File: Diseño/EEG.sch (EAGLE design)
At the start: 32 parts, among them IC1 REF2033AIDDCT, IC2 MCP73831T-2ACI_OT, IC3 LP38692MP-3.3_NOPB, X1 MINI-USB_4P-85-32004-40X

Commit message: correcciones
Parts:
- removed X1: MINI-USB_4P-85-32004-40X, con-cypressindustries:MINI-USB_4P-85-32004-40X
- added J1: USB3500-30-A-KIT, USB3500-30-A-KIT:USB3500-30-A-KIT
- added J2: SJ3-35083A-TR, SJ3-35083A-TR:SJ3-35083A-TR
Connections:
- new net CS1: INA_1.-IN, J2.TIP
- new net CS2: INA_1.+IN, J2.RING
- net +BATT: no longer X1.1
- net GND: now also J1.MH1, J1.MH2, J1.MH3, J1.MH4, J2.SLEEVE; no longer X1.4
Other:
- moved on the sheet: C1, C3, IC2, LED1, R1, R2

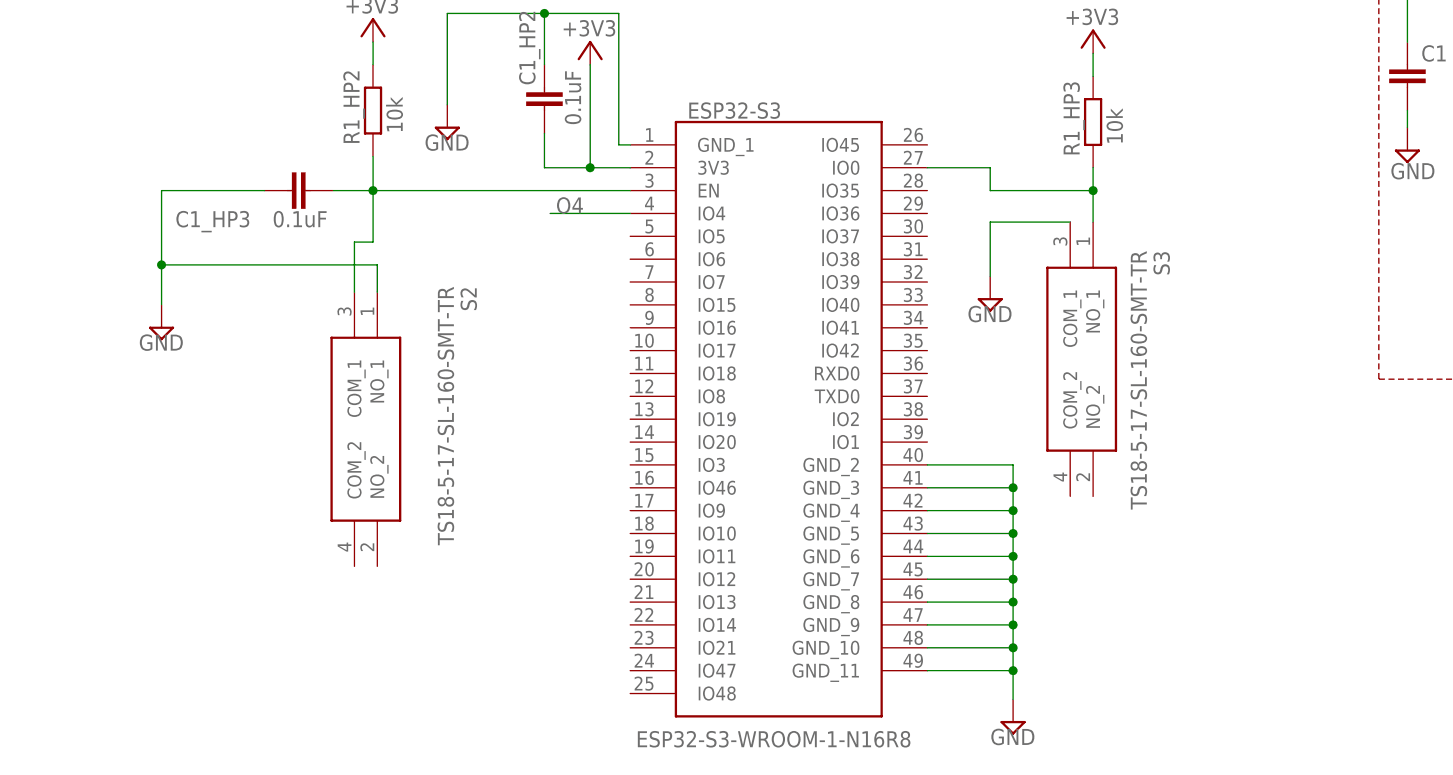
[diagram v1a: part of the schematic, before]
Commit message: Se actualizo el diagrama de la ESP 32-S3
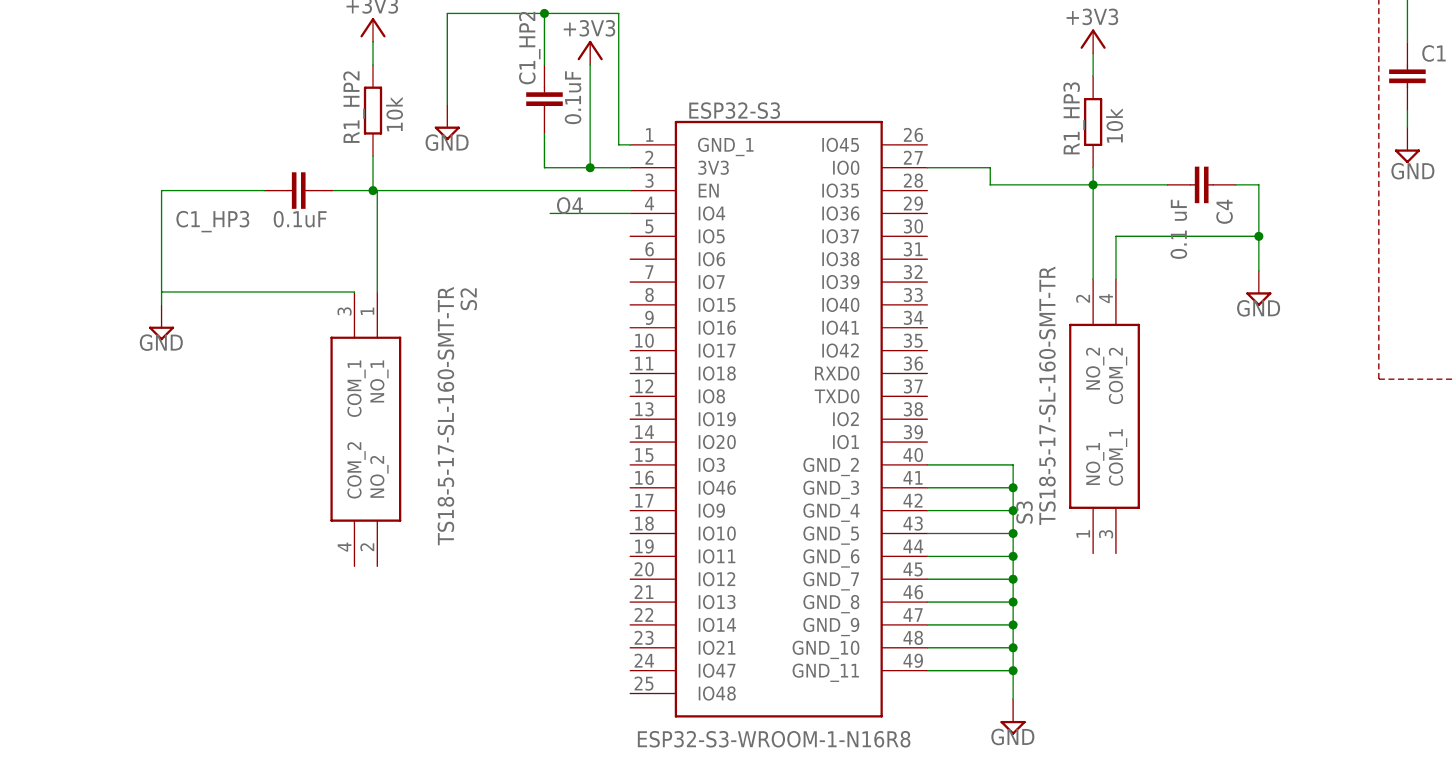
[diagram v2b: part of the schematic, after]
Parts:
- added C4: 0.1 uF, rcl:C-EUC0805
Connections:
- net GND: now also C4.1, S2.COM_1, S3.COM_2; no longer S2.NO_1, S3.COM_1
- net N$13: now also C4.2, S3.NO_2; no longer S3.NO_1
- net N$15: now also S2.NO_1; no longer S2.COM_1
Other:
- moved on the sheet: S3
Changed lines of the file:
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@@
 <part name="SUPPLY15" library="supply2" library_urn="urn:adsk.eagle:library:372" deviceset="GND" device=""/>
 <part name="GND6" library="supply2" library_urn="urn:adsk.eagle:library:372" deviceset="GND" device=""/>
+<part name="C4" library="rcl" library_urn="urn:adsk.eagle:library:334" deviceset="C-EU" device="C0805" package3d_urn="urn:adsk.eagle:package:23617/2" value="0.1 uF"/>
 </parts>
 <sheets>
@@
 <attribute name="VALUE" x="48.73625" y="61.11875" size="1.778" layer="96" rot="R270" align="center-left"/>
 </instance>
-<instance part="S3" gate="G$1" x="120.65" y="68.2625" smashed="yes" rot="R270">
-<attribute name="NAME" x="128.27" y="65.0875" size="1.778" layer="95" rot="R270" align="center-left"/>
-<attribute name="VALUE" x="125.73" y="65.0875" size="1.778" layer="96" rot="R270" align="center-left"/>
+<instance part="S3" gate="G$1" x="120.65" y="31.4325" smashed="yes" rot="R90">
+<attribute name="NAME" x="113.03" y="34.6075" size="1.778" layer="95" rot="R90" align="center-left"/>
+<attribute name="VALUE" x="115.57" y="34.6075" size="1.778" layer="96" rot="R90" align="center-left"/>
 </instance>
 <instance part="R1_HP2" gate="G$1" x="40.64" y="80.645" smashed="yes" rot="R90">
@@
 <attribute name="VALUE" x="117.475" y="90.17" size="1.778" layer="96"/>
 </instance>
-<instance part="GND4" gate="GND" x="109.22" y="59.69" smashed="yes">
-<attribute name="VALUE" x="106.68" y="57.15" size="1.778" layer="96"/>
+<instance part="GND4" gate="GND" x="139.065" y="60.325" smashed="yes">
+<attribute name="VALUE" x="136.525" y="57.785" size="1.778" layer="96"/>
 </instance>
 <instance part="GND5" gate="GND" x="111.76" y="12.7" smashed="yes">
@@
 <instance part="GND6" gate="GND" x="8.89" y="137.795" smashed="yes">
 <attribute name="VALUE" x="6.35" y="135.255" size="1.778" layer="96"/>
+</instance>
+<instance part="C4" gate="G$1" x="133.985" y="72.39" smashed="yes" rot="R270">
+<attribute name="NAME" x="134.366" y="70.866" size="1.778" layer="95" rot="R270"/>
+<attribute name="VALUE" x="129.286" y="70.866" size="1.778" layer="96" rot="R270"/>
 </instance>
 </instances>
@@
 <pinref part="GND3" gate="GND" pin="GND"/>
 <wire x1="28.575" y1="71.755" x2="17.145" y2="71.755" width="0.1524" layer="91"/>
-<wire x1="17.145" y1="71.755" x2="17.145" y2="63.5" width="0.1524" layer="91"/>
-<pinref part="S2" gate="G$1" pin="NO_1"/>
-<wire x1="17.145" y1="63.5" x2="17.145" y2="59.055" width="0.1524" layer="91"/>
-<wire x1="41.11625" y1="60.48375" x2="41.11625" y2="63.5" width="0.1524" layer="91"/>
-<wire x1="41.11625" y1="63.5" x2="17.145" y2="63.5" width="0.1524" layer="91"/>
-<junction x="17.145" y="63.5"/>
-</segment>
-<segment>
-<pinref part="S3" gate="G$1" pin="COM_1"/>
-<wire x1="118.11" y1="68.2625" x2="109.22" y2="68.2625" width="0.1524" layer="91"/>
-<pinref part="GND4" gate="GND" pin="GND"/>
-<wire x1="109.22" y1="68.2625" x2="109.22" y2="62.23" width="0.1524" layer="91"/>
+<wire x1="17.145" y1="71.755" x2="17.145" y2="60.48375" width="0.1524" layer="91"/>
+<pinref part="S2" gate="G$1" pin="COM_1"/>
+<wire x1="17.145" y1="60.325" x2="17.145" y2="59.055" width="0.1524" layer="91"/>
+<wire x1="38.57625" y1="60.48375" x2="17.145" y2="60.48375" width="0.1524" layer="91"/>
+<wire x1="17.145" y1="60.48375" x2="17.145" y2="60.325" width="0.1524" layer="91"/>
 </segment>
 <segment>
@@
 <wire x1="18.415" y1="141.605" x2="8.89" y2="141.605" width="0.1524" layer="91"/>
 </segment>
+<segment>
+<pinref part="GND4" gate="GND" pin="GND"/>
+<pinref part="C4" gate="G$1" pin="1"/>
+<wire x1="139.065" y1="62.865" x2="139.065" y2="66.675" width="0.1524" layer="91"/>
+<wire x1="139.065" y1="66.675" x2="139.065" y2="72.39" width="0.1524" layer="91"/>
+<wire x1="139.065" y1="72.39" x2="136.525" y2="72.39" width="0.1524" layer="91"/>
+<pinref part="S3" gate="G$1" pin="COM_2"/>
+<wire x1="123.19" y1="61.9125" x2="123.19" y2="66.675" width="0.1524" layer="91"/>
+<wire x1="123.19" y1="66.675" x2="139.065" y2="66.675" width="0.1524" layer="91"/>
+<junction x="139.065" y="66.675"/>
+</segment>
 </net>
 <net name="N$1" class="0">
@@
 <pinref part="R1_HP2" gate="G$1" pin="1"/>
 <wire x1="40.64" y1="71.755" x2="40.64" y2="75.565" width="0.1524" layer="91"/>
-<pinref part="S2" gate="G$1" pin="COM_1"/>
-<wire x1="38.57625" y1="60.48375" x2="38.57625" y2="66.04" width="0.1524" layer="91"/>
-<wire x1="38.57625" y1="66.04" x2="40.64" y2="66.04" width="0.1524" layer="91"/>
-<wire x1="40.64" y1="66.04" x2="40.64" y2="71.755" width="0.1524" layer="91"/>
-</segment>
-</net>
-<net name="N$13" class="0">
-<segment>
-<pinref part="S3" gate="G$1" pin="NO_1"/>
-<pinref part="R1_HP3" gate="G$1" pin="1"/>
-<wire x1="120.65" y1="68.2625" x2="120.65" y2="71.755" width="0.1524" layer="91"/>
-<pinref part="ESP32-S3" gate="G$1" pin="IO0"/>
-<wire x1="120.65" y1="71.755" x2="120.65" y2="74.295" width="0.1524" layer="91"/>
-<wire x1="102.235" y1="74.295" x2="109.22" y2="74.295" width="0.1524" layer="91"/>
-<wire x1="109.22" y1="74.295" x2="109.22" y2="71.755" width="0.1524" layer="91"/>
-<wire x1="109.22" y1="71.755" x2="120.65" y2="71.755" width="0.1524" layer="91"/>
-<junction x="120.65" y="71.755"/>
+<pinref part="S2" gate="G$1" pin="NO_1"/>
+<wire x1="41.11625" y1="60.48375" x2="41.11625" y2="71.755" width="0.1524" layer="91"/>
+<wire x1="41.11625" y1="71.755" x2="40.64" y2="71.755" width="0.1524" layer="91"/>
 </segment>
 </net>
@@
 </segment>
 </net>
+<net name="N$13" class="0">
+<segment>
+<pinref part="ESP32-S3" gate="G$1" pin="IO0"/>
+<wire x1="102.235" y1="74.295" x2="109.22" y2="74.295" width="0.1524" layer="91"/>
+<wire x1="109.22" y1="74.295" x2="109.22" y2="72.39" width="0.1524" layer="91"/>
+<pinref part="C4" gate="G$1" pin="2"/>
+<wire x1="109.22" y1="72.39" x2="120.65" y2="72.39" width="0.1524" layer="91"/>
+<wire x1="120.65" y1="72.39" x2="128.905" y2="72.39" width="0.1524" layer="91"/>
+<junction x="120.65" y="72.39"/>
+<pinref part="R1_HP3" gate="G$1" pin="1"/>
+<wire x1="120.65" y1="74.295" x2="120.65" y2="72.39" width="0.1524" layer="91"/>
+<pinref part="S3" gate="G$1" pin="NO_2"/>
+<wire x1="120.65" y1="61.9125" x2="120.65" y2="72.39" width="0.1524" layer="91"/>
+</segment>
+</net>

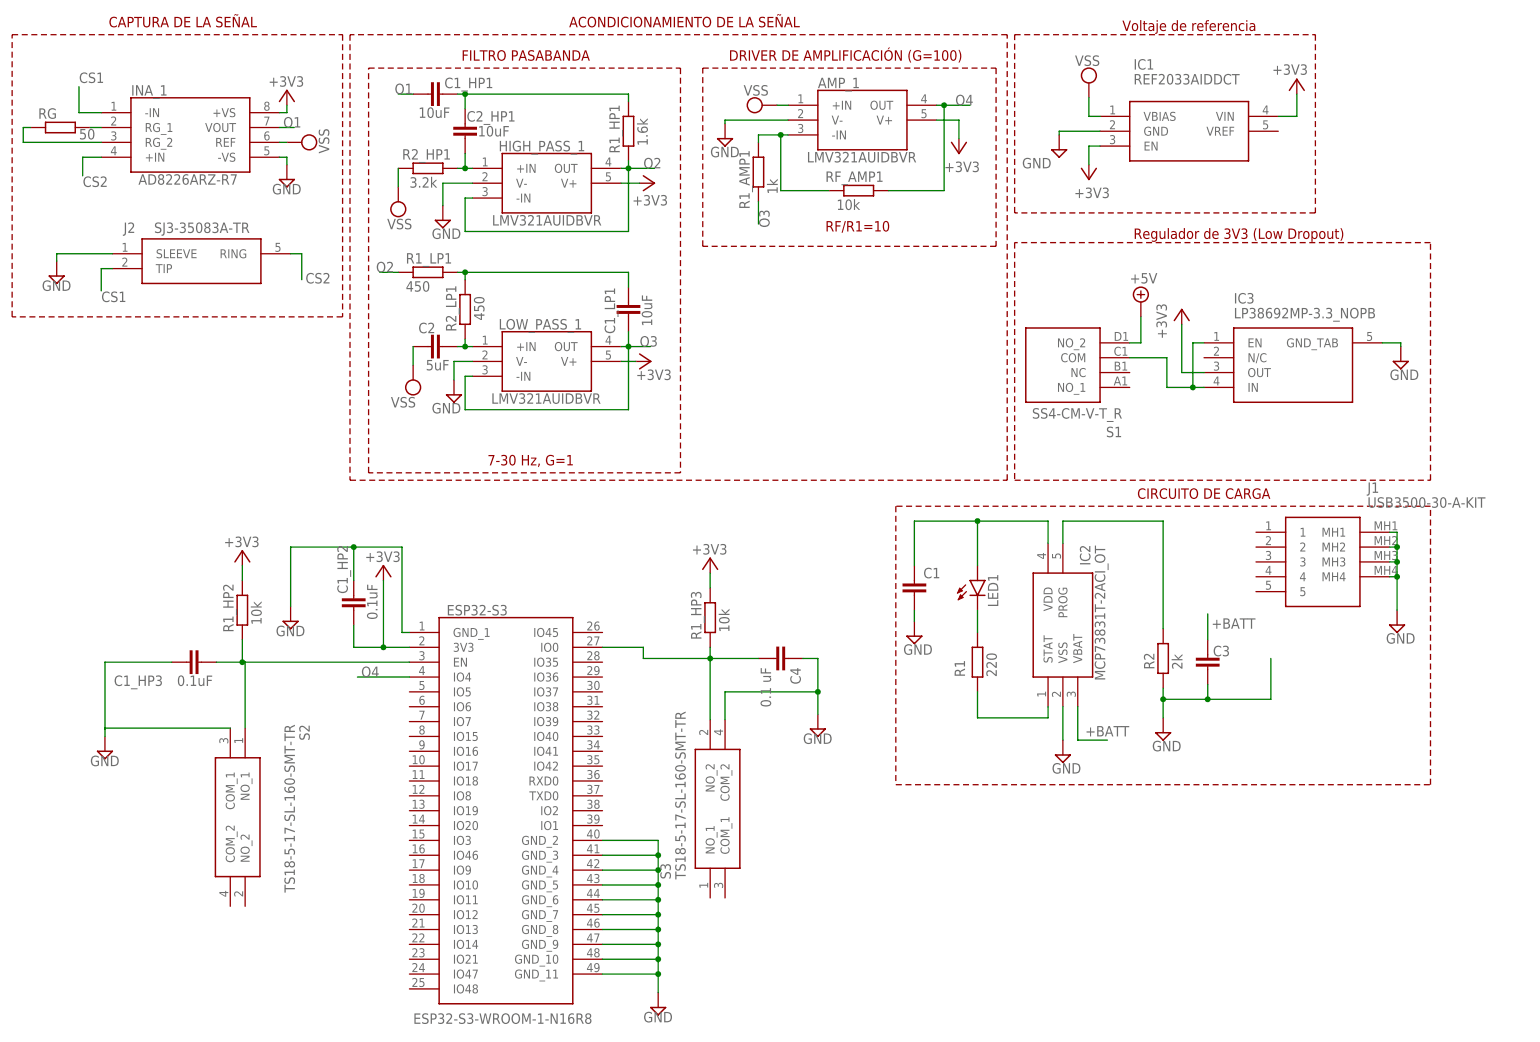
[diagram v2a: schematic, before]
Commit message: mod circuito de carga, amplificadores y filtros
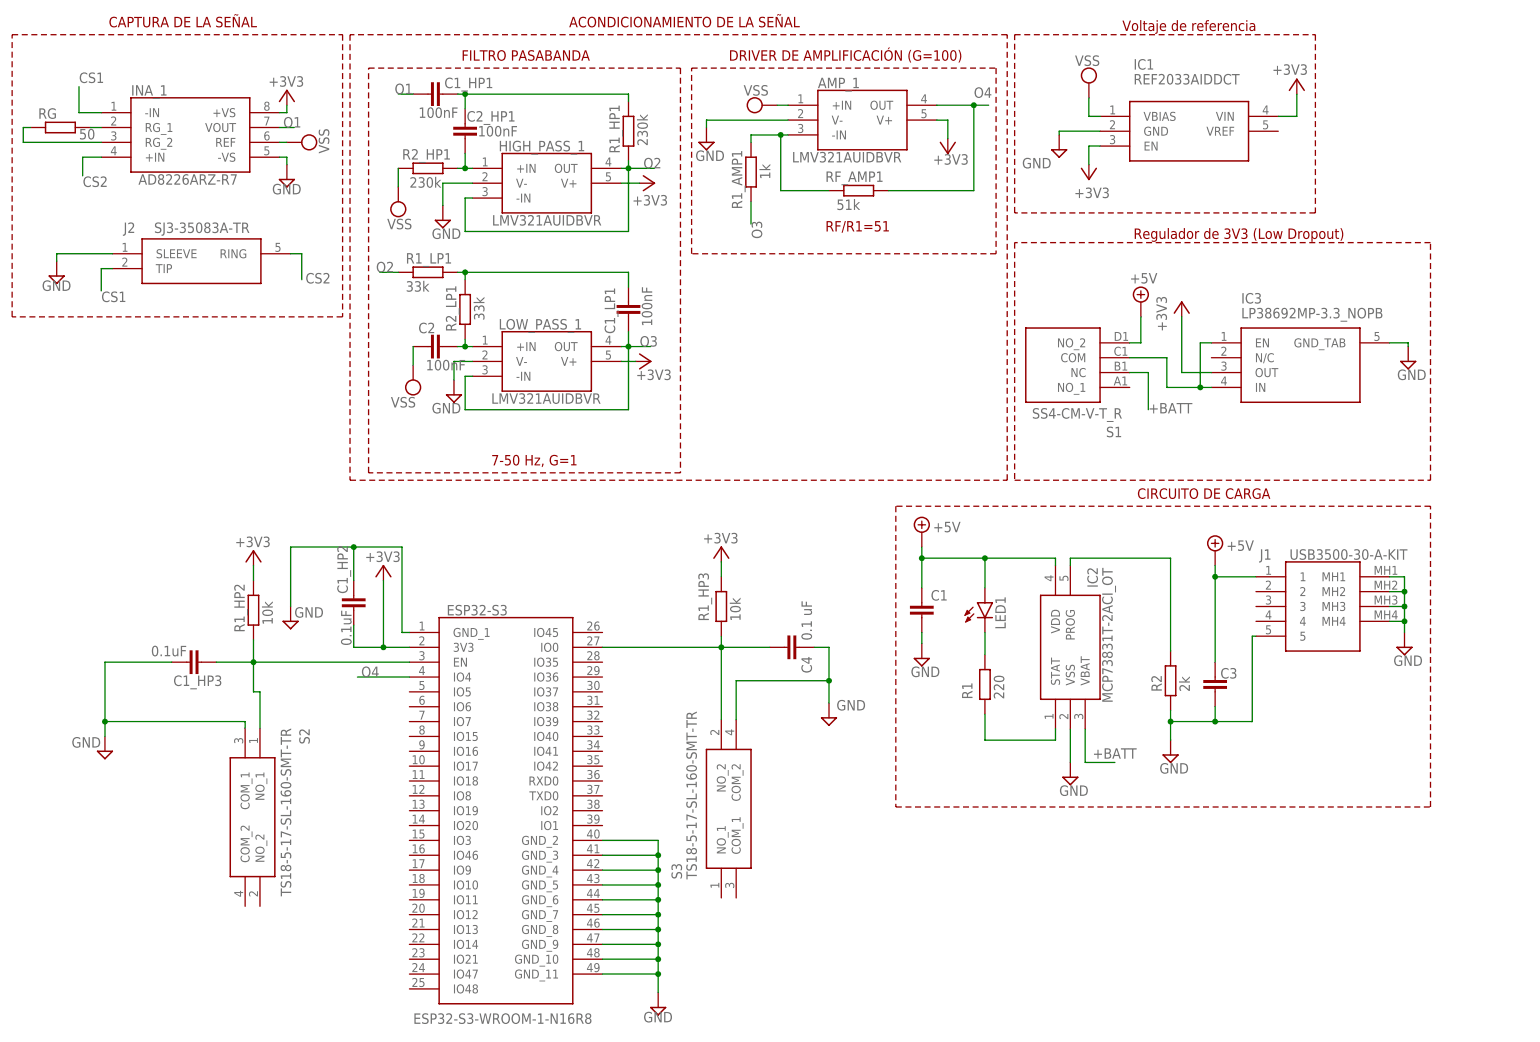
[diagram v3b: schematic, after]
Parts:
- C1_HP1, C1_LP1, C2_HP1: value 10uF -> 100nF
- C2: value 5uF -> 100nF
- R1_HP1: value 1.6k -> 230k
- R1_LP1, R2_LP1: value 450 -> 33k
- R2_HP1: value 3.2k -> 230k
- RF_AMP1: value 10k -> 51k
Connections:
- removed net N$1: C1.1, IC2.VDD, LED1.A
- net +5V: now also C1.1, C3.1, IC2.VDD, J1.1, LED1.A
- net +BATT: now also S1.NC; no longer C3.1
- net GND: now also J1.5
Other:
- note added: "7-50 Hz, G=1"
- note added: "RF/R1=51"
- note removed: "7-30 Hz, G=1"
- note removed: "RF/R1=10"
- moved on the sheet: C1, C3, C4, IC2, IC3, J1, LED1, R1, R1_AMP1, R1_HP2, R1_HP3, R2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
